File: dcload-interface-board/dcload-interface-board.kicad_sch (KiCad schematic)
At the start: 8 parts, among them J1 Conn_02x06_Odd_Even

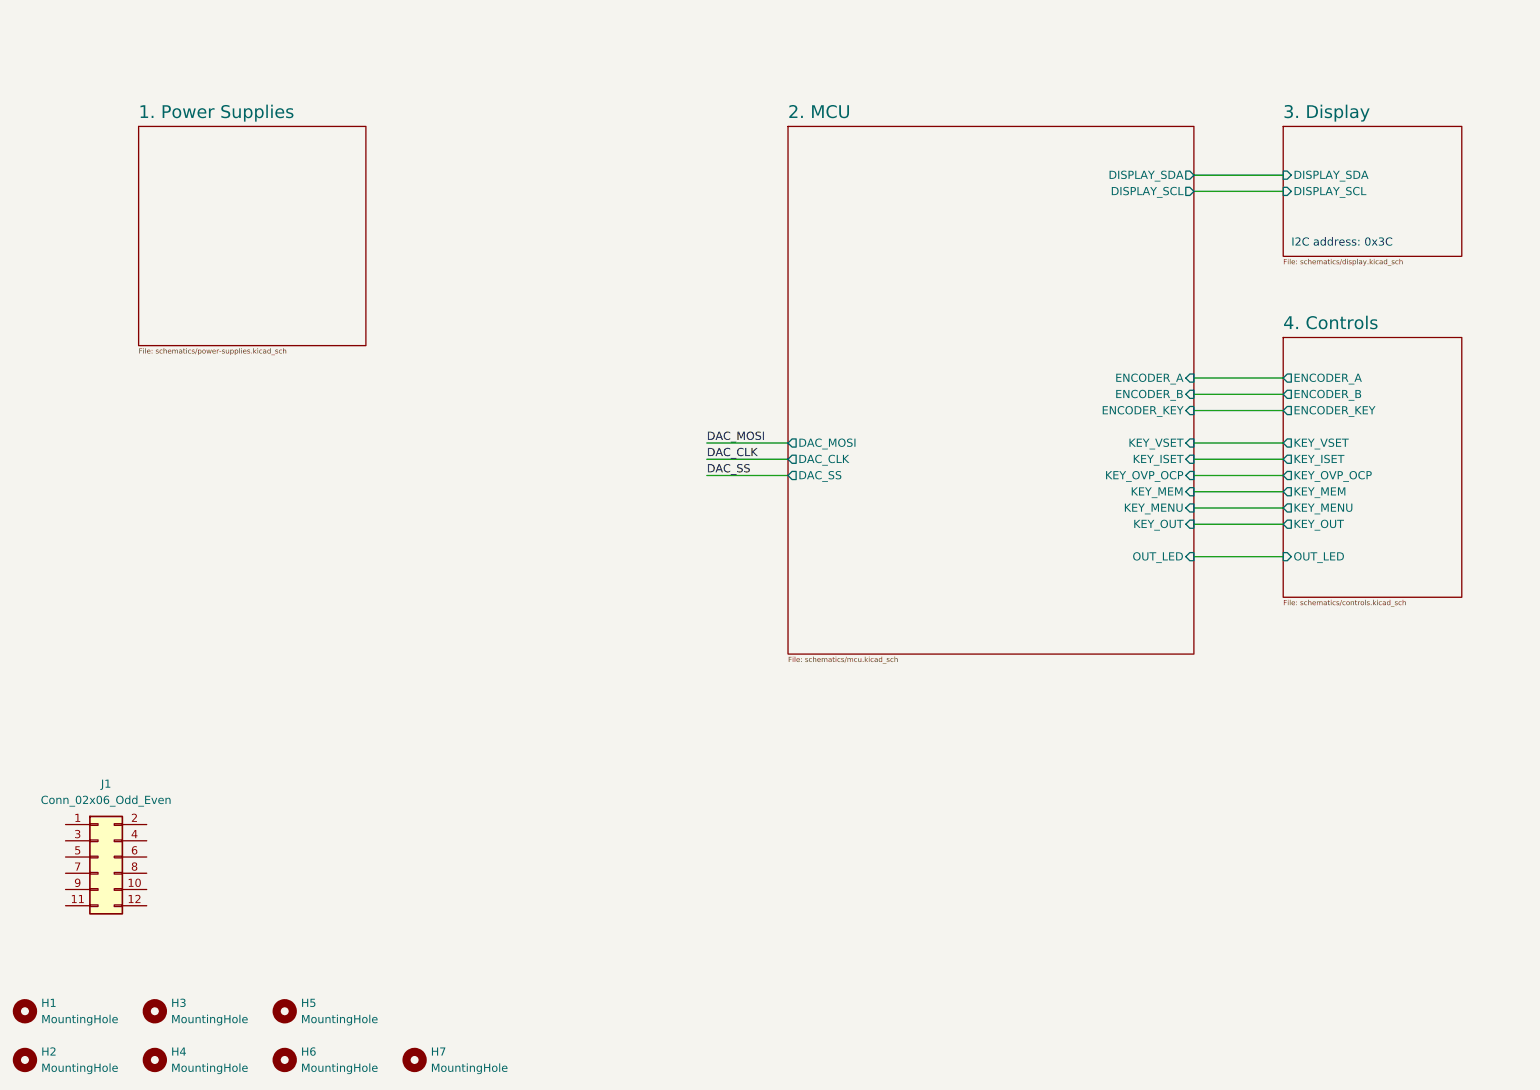
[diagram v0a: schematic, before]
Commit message: add: interface panel board
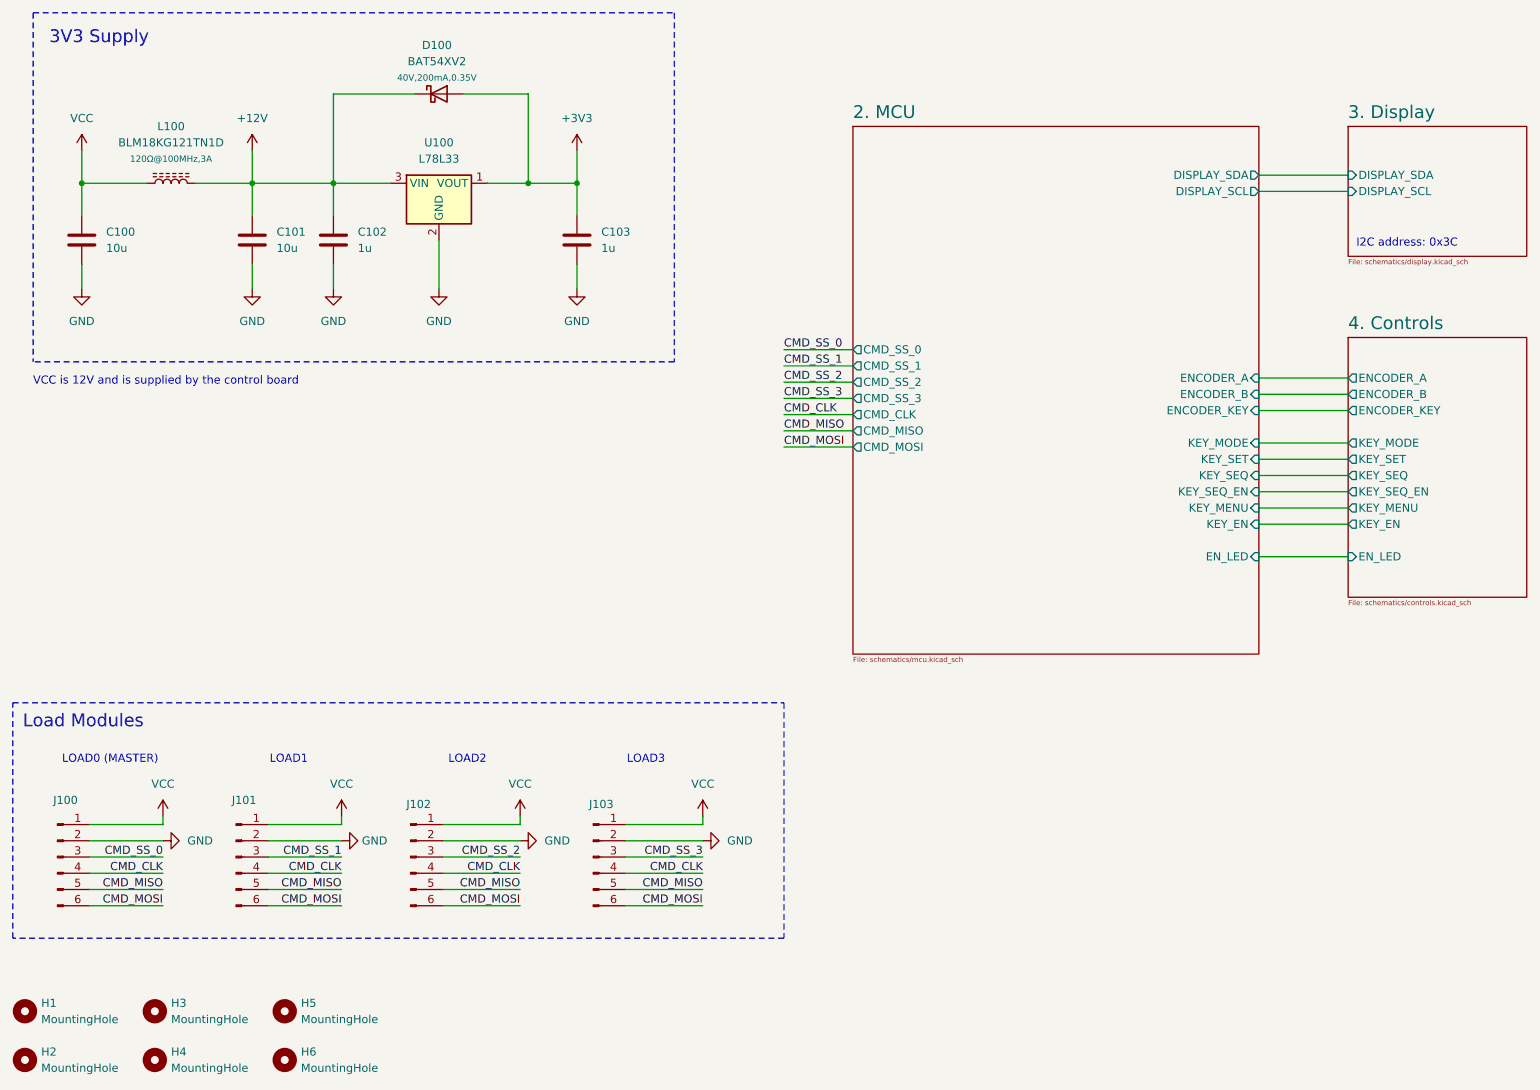
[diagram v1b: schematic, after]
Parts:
- removed H2: MountingHole, MountingHole:MountingHole_3.2mm_M3, symbol Mechanical:MountingHole
- removed J1: Conn_02x06_Odd_Even, Connector_PinHeader_2.54mm:PinHeader_2x06_P2.54mm_Vertical_SMD, symbol Connector_Generic:Conn_02x06_Odd_Even
- added C100, C101: 10u, Capacitor_SMD:C_0603_1608Metric, symbol Device:C
- added C102, C103: 1u, Capacitor_SMD:C_0603_1608Metric, symbol Device:C
- added D100: BAT54XV2, w-diode:SOD-523, symbol w-diode:BAT54XV2
- added J100, J101, J102, J103: Conn_01x06_Male, Connector_PinHeader_2.54mm:PinHeader_1x06_P2.54mm_Vertical, symbol Connector:Conn_01x06_Male
- added L100: BLM18KG121TN1D, Resistor_SMD:R_0603_1608Metric, symbol Device:L_Ferrite
- added U100: L78L33, w-ic:SOT-89-3, symbol w-regulator:L78Lxx
- renumbered H7 to H2
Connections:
- new net +12V: C101.1, C102.1, D100.1 (K), L100.2, U100.3 (VIN)
- new net +3V3: C103.1, D100.2 (A), U100.1 (VOUT)
- new net CMD_CLK: J100.4 (Pin_4), J101.4 (Pin_4), J102.4 (Pin_4), J103.4 (Pin_4)
- new net CMD_MISO: J100.5 (Pin_5), J101.5 (Pin_5), J102.5 (Pin_5), J103.5 (Pin_5)
- new net CMD_MOSI: J100.6 (Pin_6), J101.6 (Pin_6), J102.6 (Pin_6), J103.6 (Pin_6)
- new net CMD_SS_0: J100.3 (Pin_3)
- new net CMD_SS_1: J101.3 (Pin_3)
- new net CMD_SS_2: J102.3 (Pin_3)
- new net CMD_SS_3: J103.3 (Pin_3)
- new net GND: C100.2, C101.2, C102.2, C103.2, J100.2 (Pin_2), J101.2 (Pin_2), J102.2 (Pin_2), J103.2 (Pin_2), U100.2 (GND)
- new net VCC: C100.1, J100.1 (Pin_1), J101.1 (Pin_1), J102.1 (Pin_1), J103.1 (Pin_1), L100.1
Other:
- removed sheet 1. Power Supplies
- sheet 2. MCU ports: added CMD_CLK, CMD_MISO, CMD_MOSI, CMD_SS_0, CMD_SS_1, CMD_SS_2, CMD_SS_3, EN_LED, KEY_EN, KEY_MODE, KEY_SEQ, KEY_SEQ_EN, KEY_SET; removed DAC_CLK, DAC_MOSI, DAC_SS, KEY_ISET, KEY_MEM, KEY_OUT, KEY_OVP_OCP, KEY_VSET, OUT_LED
- sheet 4. Controls ports: added EN_LED, KEY_EN, KEY_MODE, KEY_SEQ, KEY_SEQ_EN, KEY_SET; removed KEY_ISET, KEY_MEM, KEY_OUT, KEY_OVP_OCP, KEY_VSET, OUT_LED
- note added: "3V3 Supply"
- note added: "LOAD0 (MASTER)"
- note added: "LOAD1"
- note added: "LOAD2"
- note added: "LOAD3"
- note added: "VCC is 12V and is supplied by the control board"
- moved on the sheet: H2
